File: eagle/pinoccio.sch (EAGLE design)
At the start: 61 parts, among them IC1 ATMEGA16U2QFN32, J1 AVR_SPI_PRG_6, Q1 16MHz, Q2 32.768k, Q3 16MHz, U1 MCP73831, U2 3.3V, U4 ATMEGA128RFA1, X1 USB-MICROB, Y2 ANTENNA2SMD5

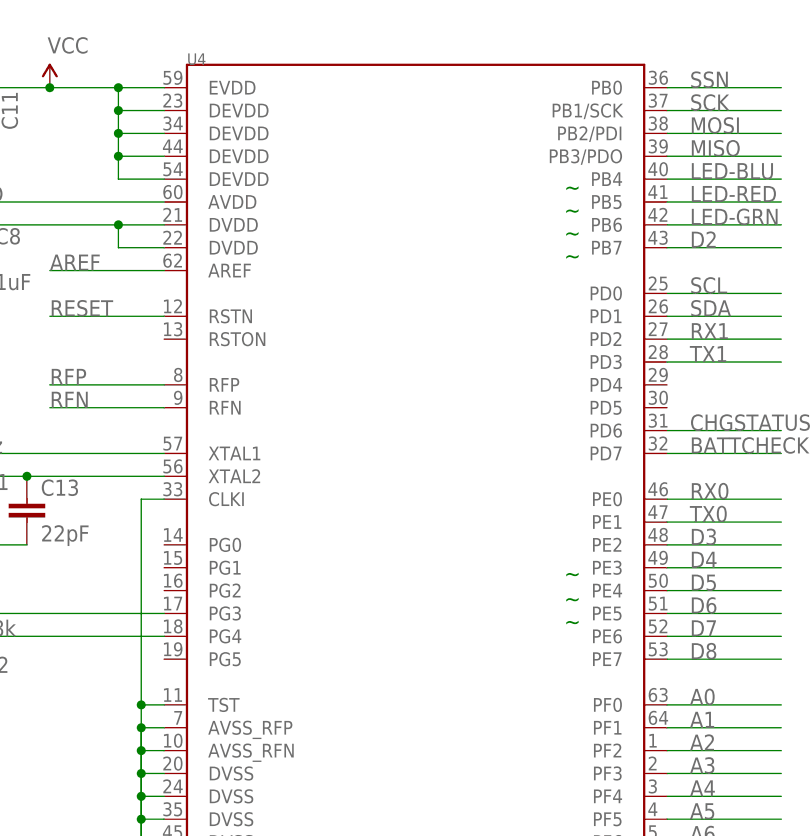
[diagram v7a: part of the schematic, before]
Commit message: Updated rfa1 with PWM and interrupt notes
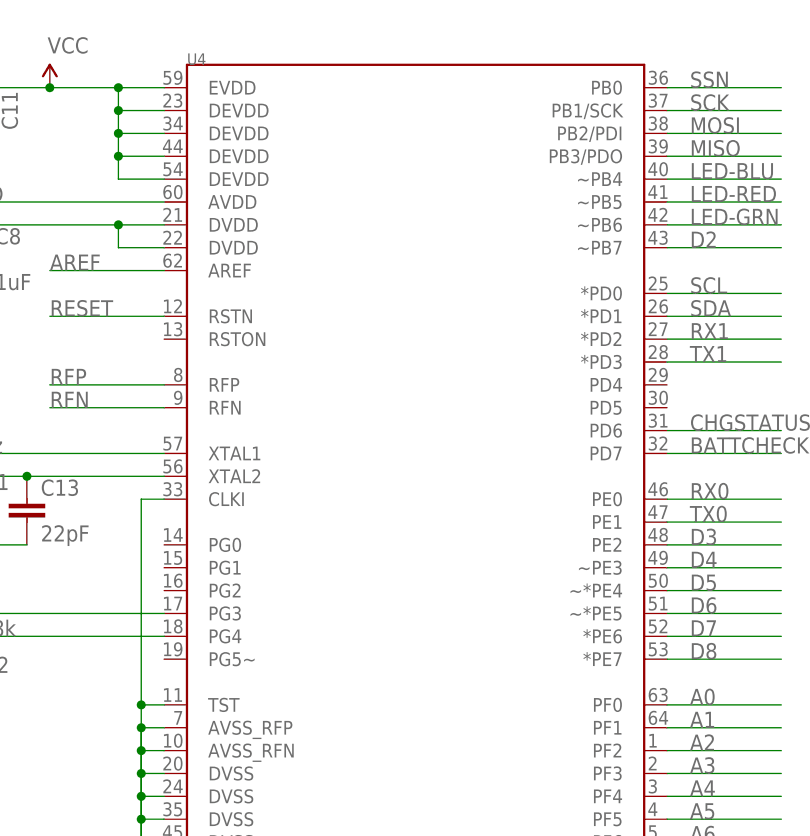
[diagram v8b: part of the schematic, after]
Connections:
- net D2: now also U4.~PB7; no longer U4.PB7
- net D4: now also U4.~PE3; no longer U4.PE3
- net D5: now also U4.~*PE4; no longer U4.PE4
- net D6: now also U4.~*PE5; no longer U4.PE5
- net D7: now also U4.*PE6; no longer U4.PE6
- net D8: now also U4.*PE7; no longer U4.PE7
- net LED-BLU: now also U4.~PB4; no longer U4.PB4
- net LED-GRN: now also U4.~PB6; no longer U4.PB6
- net LED-RED: now also U4.~PB5; no longer U4.PB5
- net RX1: now also U4.*PD2; no longer U4.PD2
- net SCL: now also U4.*PD0; no longer U4.PD0
- net SDA: now also U4.*PD1; no longer U4.PD1
- net TX1: now also U4.*PD3; no longer U4.PD3
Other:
- note removed: "~"
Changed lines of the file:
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@@
 <text x="2.54" y="170.18" size="1.778" layer="95">INCLUDING OF MERCHANTABILITY, SATISFACTORY QUALITY AND FITNESS FOR A</text>
 <text x="2.54" y="167.64" size="1.778" layer="95">PARTICULAR PURPOSE. Please see the CERN OHL v.1.1 for applicable conditions</text>
-<text x="189.23" y="122.936" size="1.778" layer="91">~</text>
-<text x="189.23" y="120.142" size="1.778" layer="91">~</text>
-<text x="189.23" y="117.602" size="1.778" layer="91">~</text>
-<text x="189.23" y="165.862" size="1.778" layer="91">~</text>
-<text x="189.23" y="163.322" size="1.778" layer="91">~</text>
-<text x="189.23" y="160.782" size="1.778" layer="91">~</text>
-<text x="189.23" y="158.242" size="1.778" layer="91">~</text>
 </plain>
 <instances>
@@
 <wire x1="213.36" y1="149.86" x2="200.66" y2="149.86" width="0.1524" layer="91"/>
 <label x="203.2" y="149.86" size="1.778" layer="95"/>
-<pinref part="U4" gate="G$1" pin="PD2"/>
+<pinref part="U4" gate="G$1" pin="*PD2"/>
 </segment>
 <segment>
@@
 <wire x1="213.36" y1="147.32" x2="200.66" y2="147.32" width="0.1524" layer="91"/>
 <label x="203.2" y="147.32" size="1.778" layer="95"/>
-<pinref part="U4" gate="G$1" pin="PD3"/>
+<pinref part="U4" gate="G$1" pin="*PD3"/>
 </segment>
 <segment>
@@
 </segment>
 <segment>
-<pinref part="U4" gate="G$1" pin="PB7"/>
+<pinref part="U4" gate="G$1" pin="~PB7"/>
 <wire x1="200.66" y1="160.02" x2="213.36" y2="160.02" width="0.1524" layer="91"/>
 <label x="203.2" y="160.02" size="1.778" layer="95"/>
@@
 </segment>
 <segment>
-<pinref part="U4" gate="G$1" pin="PE3"/>
+<pinref part="U4" gate="G$1" pin="~PE3"/>
 <wire x1="200.66" y1="124.46" x2="213.36" y2="124.46" width="0.1524" layer="91"/>
 <label x="203.2" y="124.46" size="1.778" layer="95"/>
@@
 </segment>
 <segment>
-<pinref part="U4" gate="G$1" pin="PE4"/>
+<pinref part="U4" gate="G$1" pin="~*PE4"/>
 <wire x1="200.66" y1="121.92" x2="213.36" y2="121.92" width="0.1524" layer="91"/>
 <label x="203.2" y="121.92" size="1.778" layer="95"/>
@@
 </segment>
 <segment>
-<pinref part="U4" gate="G$1" pin="PE5"/>
+<pinref part="U4" gate="G$1" pin="~*PE5"/>
 <wire x1="200.66" y1="119.38" x2="213.36" y2="119.38" width="0.1524" layer="91"/>
 <label x="203.2" y="119.38" size="1.778" layer="95"/>
@@
 </segment>
 <segment>
-<pinref part="U4" gate="G$1" pin="PE7"/>
+<pinref part="U4" gate="G$1" pin="*PE7"/>
 <wire x1="200.66" y1="114.3" x2="213.36" y2="114.3" width="0.1524" layer="91"/>
 <label x="203.2" y="114.3" size="1.778" layer="95"/>
@@
 </segment>
 <segment>
-<pinref part="U4" gate="G$1" pin="PE6"/>
+<pinref part="U4" gate="G$1" pin="*PE6"/>
 <wire x1="200.66" y1="116.84" x2="213.36" y2="116.84" width="0.1524" layer="91"/>
 <label x="203.2" y="116.84" size="1.778" layer="95"/>
@@
 <segment>
 <wire x1="213.36" y1="154.94" x2="200.66" y2="154.94" width="0.1524" layer="91"/>
-<pinref part="U4" gate="G$1" pin="PD0"/>
+<pinref part="U4" gate="G$1" pin="*PD0"/>
 <label x="203.2" y="154.94" size="1.778" layer="95"/>
 </segment>
@@
 <segment>
 <wire x1="213.36" y1="152.4" x2="200.66" y2="152.4" width="0.1524" layer="91"/>
-<pinref part="U4" gate="G$1" pin="PD1"/>
+<pinref part="U4" gate="G$1" pin="*PD1"/>
 <label x="203.2" y="152.4" size="1.778" layer="95"/>
 </segment>
@@
 </segment>
 <segment>
-<pinref part="U4" gate="G$1" pin="PB5"/>
+<pinref part="U4" gate="G$1" pin="~PB5"/>
 <wire x1="200.66" y1="165.1" x2="213.36" y2="165.1" width="0.1524" layer="91"/>
 <label x="203.2" y="165.1" size="1.778" layer="95"/>
@@
 </segment>
 <segment>
-<pinref part="U4" gate="G$1" pin="PB6"/>
+<pinref part="U4" gate="G$1" pin="~PB6"/>
 <wire x1="200.66" y1="162.56" x2="213.36" y2="162.56" width="0.1524" layer="91"/>
 <label x="203.2" y="162.56" size="1.778" layer="95"/>
@@
 </segment>
 <segment>
-<pinref part="U4" gate="G$1" pin="PB4"/>
+<pinref part="U4" gate="G$1" pin="~PB4"/>
 <wire x1="200.66" y1="167.64" x2="213.36" y2="167.64" width="0.1524" layer="91"/>
 <label x="203.2" y="167.64" size="1.778" layer="95"/>
